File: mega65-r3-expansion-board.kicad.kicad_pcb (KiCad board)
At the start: 4 copper layers, 435 x 140.6 mm, 52 parts, among them J17 C64_Tape_Port, J18 BA60BC0WT, J19 C64_User_Port, J24 Component A/V, J32 Mini-DIN-8-With-Shield, J34 Conn_01x04, J35 Conn_01x04, U16 74LVC374, U17 74LVC374, U18 74LS374, U19 74LS374, U20 74LS125, U21 74LS125, U23 74LVC374, U24 74LS125, U25 74LS374, U26 74LS374

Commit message: begin placing and routing
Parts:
- removed J32: Mini-DIN-8-With-Shield, snapeda:mini-DIN-8
- removed R38: 510R, snapeda:Labeled Resistor
- removed R39: 1K0, snapeda:Labeled Resistor
- removed R40: 2K0, snapeda:Labeled Resistor
- removed R41: 4K0, snapeda:Labeled Resistor
- removed R42, R48, R54, R60: 8K0, snapeda:Labeled Resistor
- removed R43, R49, R55, R61: 16K, snapeda:Labeled Resistor
- removed U16, U17, U23: 74LVC374, snapeda:DIP-20_LVC_Family
- removed U18, U19, U25, U26: 74LS374, snapeda:DIP-20_LS_Family
- added J1: Mini-DIN-8-With-Shield, snapeda:mini-DIN-8, F.Cu at (168.2, 41.3)
- added J2: Conn_02x06_Odd_Even, Connector_PinHeader_2.54mm:PinHeader_2x06_P2.54mm_Vertical, F.Cu at (45.6, 123.1)
- added J3: Conn_02x06_Odd_Even, Connector_PinHeader_2.54mm:PinHeader_2x06_P2.54mm_Vertical, F.Cu at (68.5, 123.1)
- added J4: Conn_02x17_Odd_Even, Connector_PinHeader_2.54mm:PinHeader_2x17_P2.54mm_Vertical, F.Cu at (120.3, 132.7)
- added J5: Conn_02x17_Odd_Even, Connector_PinHeader_2.54mm:PinHeader_2x17_P2.54mm_Vertical, F.Cu at (129.0, 133.0)
- added R1: 3K3, snapeda:Labeled Resistor, F.Cu at (123.1, 74.5)
- added R2: 3K3, snapeda:Labeled Resistor, F.Cu at (29.1, 83.7)
- added R3: 3K3, snapeda:Labeled Resistor, F.Cu at (29.1, 93.7)
- added R4: 3K3, snapeda:Labeled Resistor, F.Cu at (29.1, 60.9)
- added R5: 3K3, snapeda:Labeled Resistor, F.Cu at (29.1, 70.8)
- added R6: 3K3, snapeda:Labeled Resistor, F.Cu at (123.1, 78.6)
- added U1: 74LS595, snapeda:DIP-16_LS_Family, F.Cu at (63.4, 87.5)
- added U2: 74LS165, snapeda:DIP-16_LVC_Family, F.Cu at (63.4, 71.5)
- added U4: 74LS595, snapeda:DIP-16_LS_Family, F.Cu at (88.8, 87.5)
- added U5: 74LS165, snapeda:DIP-16_LVC_Family, F.Cu at (35.5, 100.2)
- added U6: 74LS595, snapeda:DIP-16_LS_Family, F.Cu at (142.2, 54.5)
- added U7: 74LS165, snapeda:DIP-16_LVC_Family, F.Cu at (167.6, 54.5)
- added U8: 74LS595, snapeda:DIP-16_LS_Family, F.Cu at (35.5, 87.5)
- moved J34 252.7 mm to (44.4, 108.5)
- moved J35 248.1 mm to (62.2, 108.5)
- moved R50 222.1 mm to (113.7, 49.0)
- moved R51 222.1 mm to (113.7, 52.3)
- moved R52 222.1 mm to (113.7, 55.6)
- moved R53 222.1 mm to (113.7, 58.9)
- moved U24 222.1 mm to (41.0, 51.8)
- moved H10 222.1 mm to (34.9, 47.9)
- moved H11 222.1 mm to (94.9, 47.9)
- moved H12 222.1 mm to (112.9, 37.9)
- moved H13 222.1 mm to (142.9, 37.9)
- moved H14 222.1 mm to (153.9, 37.9)
- moved H15 222.1 mm to (182.9, 37.9)
- moved H16 222.1 mm to (34.9, 107.9)
- moved H17 222.1 mm to (94.9, 107.9)
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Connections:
- J24 pad 3: AUDIO_L -> AUDIO_R
- U20 pad 1: /User Port/EN_RESET_N -> /User Port/RESET_N_O
- U20 pad 11: unconnected-(U20-Pad11) -> 1565_SERIO
- U20 pad 12: unconnected-(U20-Pad12) -> 1565_SERIO_O
- U20 pad 13: GND -> EN_1565_SERIO
- U20 pad 2: /User Port/RESET_N_O -> GND
- U20 pad 4: GND -> /User Port/ATN_O
- U20 pad 5: unconnected-(U20-Pad5) -> GND
- U20 pad 6: unconnected-(U20-Pad6) -> IEC_ATN
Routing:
- net /User Port/6V_REG_CTL: track 283.1 -> 0.00 mm, vias 7 -> 0
- net /User Port/TAPE_WRITE: track 277.6 -> 12.3 mm, vias 8 -> 1
- net /User Port/TAPE_READ: track 206.6 -> 12.4 mm, vias 6 -> 1
- net +5V: track 545.0 -> 352.5 mm, vias 12 -> 5
- net /User Port/TAPE_SENSE: track 200.3 -> 12.4 mm, vias 6 -> 1
- net 1565_SERIO: track 176.3 -> 0.00 mm, vias 3 -> 0
- net AUDIO_L: track 159.6 -> 0.00 mm, vias 1 -> 0
- net /User Port/DATA_7: track 167.1 -> 14.4 mm, vias 6 -> 0
- net MUX_DO7: track 132.6 -> 0.00 mm
- net /User Port/DATA_6: track 160.4 -> 29.0 mm, vias 8 -> 4
- net /User Port/DATA_5: track 148.0 -> 18.4 mm, vias 8 -> 1
- net MUX_DO4: track 119.3 -> 0.00 mm, vias 2 -> 0
- net FL_WDATA: track 0.00 -> 117.1 mm
- net MUX_DO3: track 115.9 -> 0.00 mm, vias 4 -> 0
- net MUX_DO2: track 113.3 -> 0.00 mm, vias 2 -> 0
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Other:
- board size 435 x 140.6 mm -> 215 x 140.6 mm
- board text removed: "."
- board text removed: "0.47uF"
- board text removed: "1N5825"
- board text removed: "22uH"
- board text removed: "J4"
- board text removed: "X"

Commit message: route many signals
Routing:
- net +5V: track 352.5 -> 565.7 mm, vias 5 -> 23
- net /User Port/RESET_N: track 23.3 -> 197.7 mm, vias 3 -> 8
- net +3V3: track 0.00 -> 133.7 mm, vias 0 -> 3
- net /User Port/PC2: track 0.00 -> 124.3 mm, vias 0 -> 3
- net /User Port/CNT2: track 0.00 -> 109.5 mm, vias 0 -> 4
- net /User Port/FLAG2: track 0.00 -> 108.7 mm, vias 0 -> 1
- net /User Port/SP1: track 0.00 -> 107.4 mm, vias 0 -> 5
- net /User Port/SP2: track 0.00 -> 100.6 mm, vias 0 -> 4
- net /User Port/CNT1: track 0.00 -> 97.3 mm, vias 0 -> 2
- net IEC_ATN: track 0.00 -> 83.4 mm, vias 0 -> 2
- net /User Port/DATA_5_O: track 0.00 -> 78.8 mm, vias 0 -> 2
- net /User Port/DATA_7_O: track 0.00 -> 77.2 mm, vias 0 -> 2
- net /User Port/EN_DATA_5: track 0.00 -> 50.0 mm, vias 0 -> 1
- net /User Port/DATA_7: track 14.4 -> 62.9 mm, vias 0 -> 5
- net /User Port/DATA_5: track 18.4 -> 65.3 mm, vias 1 -> 2
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
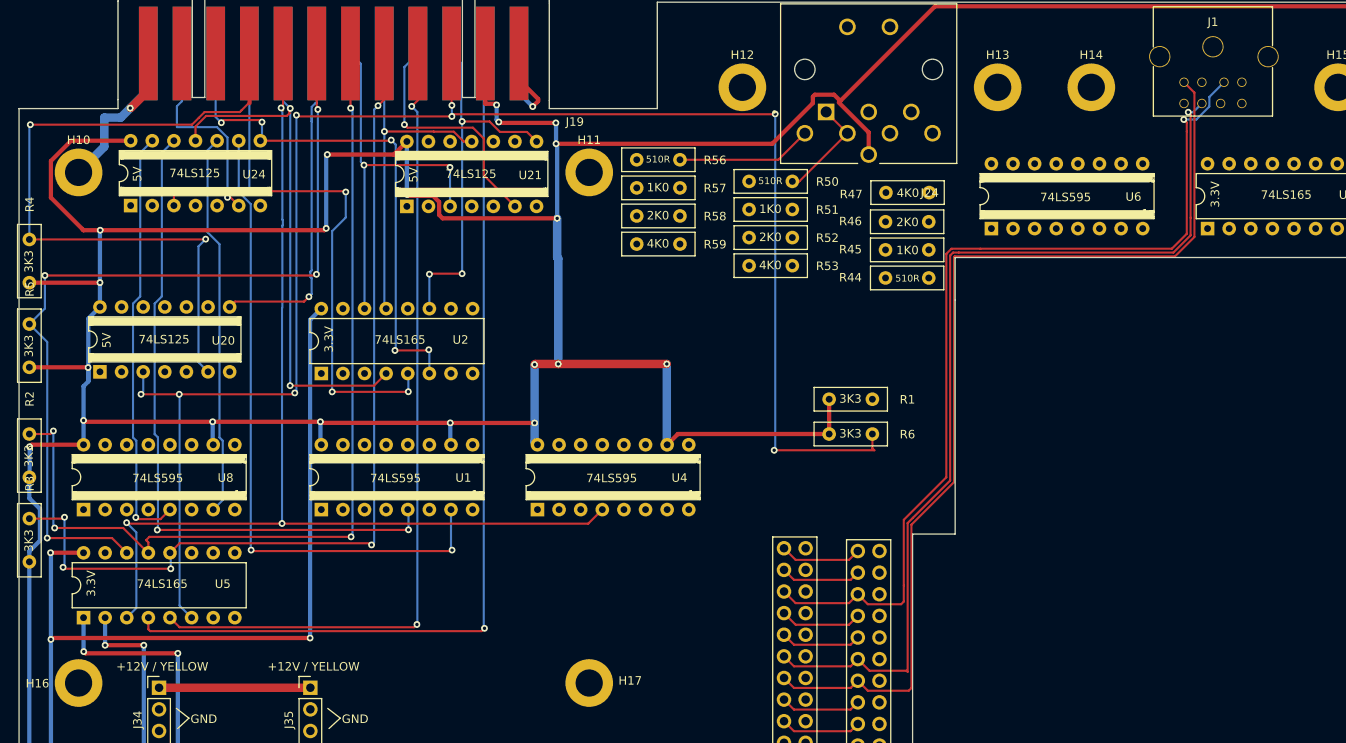
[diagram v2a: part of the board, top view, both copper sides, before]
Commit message: route many more signals
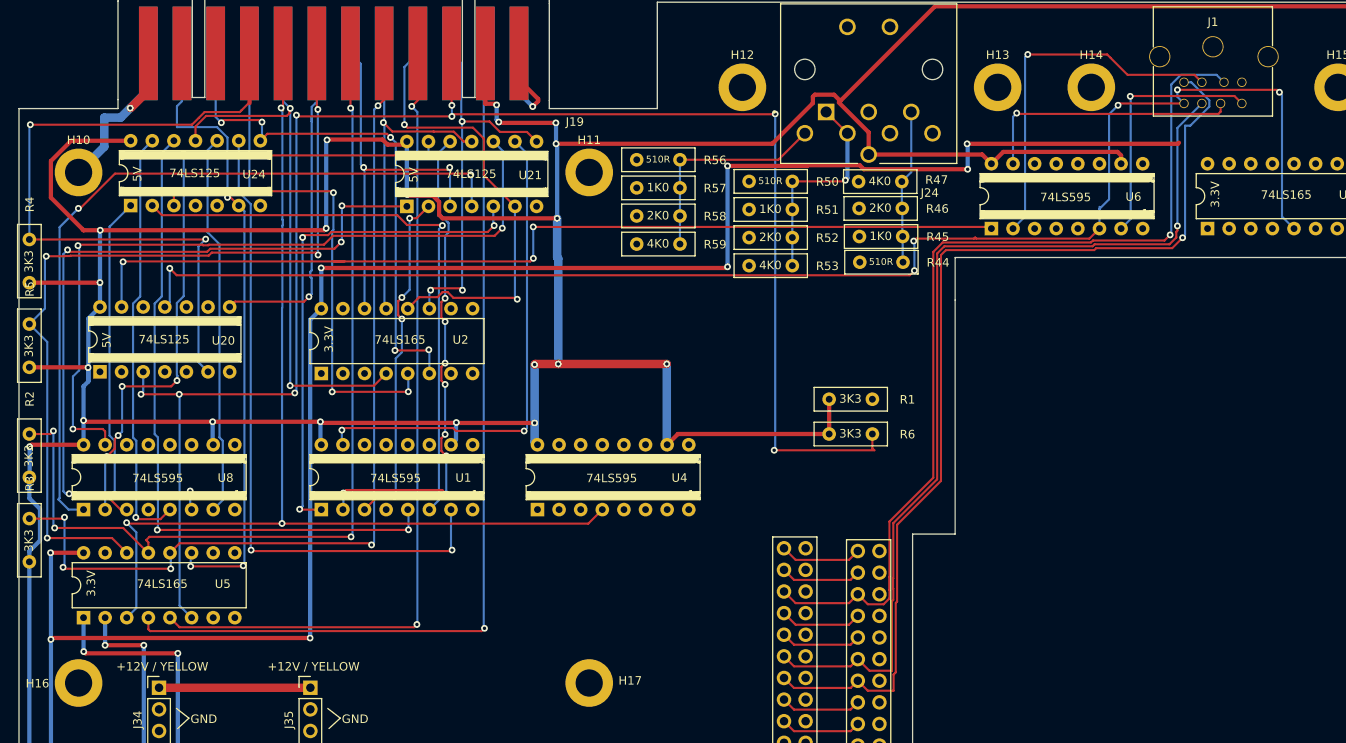
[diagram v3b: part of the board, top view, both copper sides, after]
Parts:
- moved R47 8.39 mm to (126.6, 49.0), turned to 0 degrees
- moved R46 8.34 mm to (126.6, 52.1), turned to 0 degrees
- moved R44 8.31 mm to (126.7, 58.4), turned to 0 degrees
- moved R45 8.29 mm to (126.7, 55.4), turned to 0 degrees
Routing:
- net 1565_SERIO: track 0.00 -> 173.1 mm, vias 0 -> 6
- net +3V3: track 133.7 -> 254.6 mm, vias 3 -> 8
- net EN_1565_SERIO: track 0.00 -> 112.8 mm, vias 0 -> 3
- net /User Port/EN_DATA_1: track 0.00 -> 90.4 mm, vias 0 -> 2
- net /User Port/EN_DATA_0: track 0.00 -> 88.8 mm, vias 0 -> 3
- net /User Port/EN_DATA_3: track 0.00 -> 81.6 mm, vias 0 -> 4
- net /User Port/EN_DATA_2: track 0.00 -> 79.5 mm, vias 0 -> 6
- net /User Port/DATA_6_O: track 0.00 -> 69.1 mm, vias 0 -> 1
- net /User Port/DATA_1_O: track 0.00 -> 60.0 mm, vias 0 -> 3
- net /User Port/DATA_2_O: track 0.00 -> 58.4 mm, vias 0 -> 8
- net /User Port/DATA_0_O: track 0.00 -> 58.2 mm, vias 0 -> 2
- net /User Port/PA2: track 24.1 -> 74.6 mm, vias 1 -> 3
- net /User Port/EN_DATA_6: track 0.00 -> 46.5 mm, vias 0 -> 2
- net 1565_RST: track 0.00 -> 43.0 mm, vias 0 -> 1
- net /User Port/DATA_3_O: track 0.00 -> 40.7 mm, vias 0 -> 4
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
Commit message: yet more routing
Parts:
- added U3: 74LS125, snapeda:DIP-14_74LS06, F.Cu at (88.7, 100.1)
- moved R3 2.61 mm to (29.7, 96.2)
- moved R4 2.31 mm to (29.9, 58.7)
- moved R5 1.17 mm to (30.0, 71.6)
- moved R2 0.77 mm to (29.9, 83.8)
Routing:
- net +12V_FUSED: track 17.3 -> 294.0 mm, vias 0 -> 6
- net EXP_RDATA: track 0.00 -> 274.1 mm, vias 0 -> 4
- net Net-(U5-Pad10): track 0.00 -> 217.0 mm, vias 0 -> 8
- net Net-(U6-Pad9): track 0.00 -> 158.4 mm, vias 0 -> 4
- net EXP_LATCH: track 34.2 -> 142.3 mm, vias 2 -> 10
- net EXP_CLOCK: track 27.6 -> 128.5 mm, vias 2 -> 9
- net /User Port/6V_REG_CTL: track 0.00 -> 98.4 mm, vias 0 -> 2
- net /User Port/RESET_N_O: track 0.00 -> 84.0 mm, vias 0 -> 2
- net /User Port/CNT1: track 97.3 -> 175.8 mm
- net /User Port/TAPE_WRITE: track 12.3 -> 88.8 mm, vias 1 -> 3
- net /User Port/SP2: track 100.9 -> 175.0 mm, vias 4 -> 7
- net /User Port/ATN_O: track 0.00 -> 70.9 mm, vias 0 -> 2
- net EXP_WDATA: track 0.00 -> 70.4 mm, vias 0 -> 3
- net /User Port/DATA_4_O: track 0.00 -> 59.6 mm, vias 0 -> 4
- net /User Port/TAPE_READ: track 12.4 -> 70.7 mm, vias 1 -> 3
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
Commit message: finish routing signals
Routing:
- net AUDIO_R2: track 0.00 -> 182.6 mm, vias 0 -> 2
- net AUDIO_R3: track 0.06 -> 179.9 mm, vias 0 -> 2
- net AUDIO_R4: track 0.00 -> 174.4 mm, vias 0 -> 2
- net AUDIO_R5: track 0.00 -> 168.6 mm, vias 0 -> 2
- net COMP_LUMA5: track 0.00 -> 139.1 mm, vias 0 -> 3
- net COMP_CHROMA3: track 0.00 -> 139.0 mm, vias 0 -> 4
- net COMP_CHROMA2: track 0.00 -> 138.9 mm, vias 0 -> 4
- net COMP_LUMA4: track 0.00 -> 135.3 mm, vias 0 -> 3
- net COMP_CHROMA4: track 0.00 -> 135.3 mm, vias 0 -> 4
- net COMP_LUMA3: track 0.00 -> 132.8 mm, vias 0 -> 3
- net COMP_CHROMA5: track 0.00 -> 131.0 mm, vias 0 -> 4
- net COMP_LUMA2: track 0.00 -> 127.1 mm, vias 0 -> 3
- net EXP_CLOCK: track 128.5 -> 214.4 mm, vias 9 -> 12
- net EXP_LATCH: track 142.3 -> 225.9 mm, vias 10 -> 14
- net /User Port/CNT1: track 175.8 -> 258.8 mm, vias 2 -> 6
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
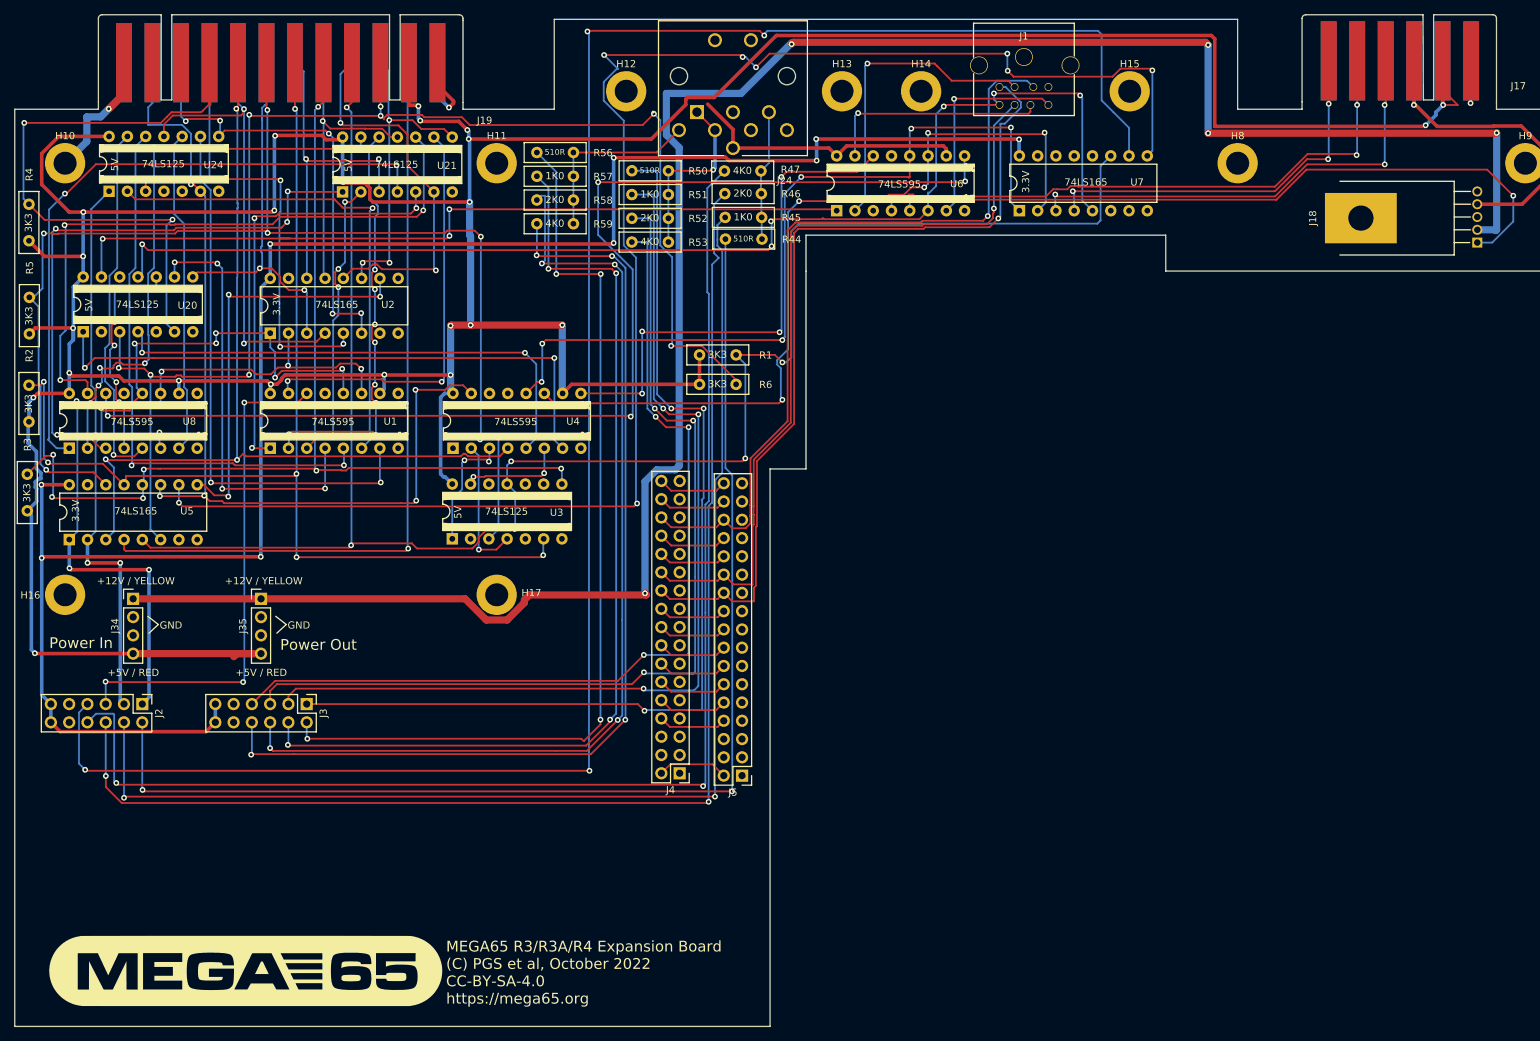
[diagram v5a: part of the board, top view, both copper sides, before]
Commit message: shrink board, resolve all DRC errors, add openhardware logo
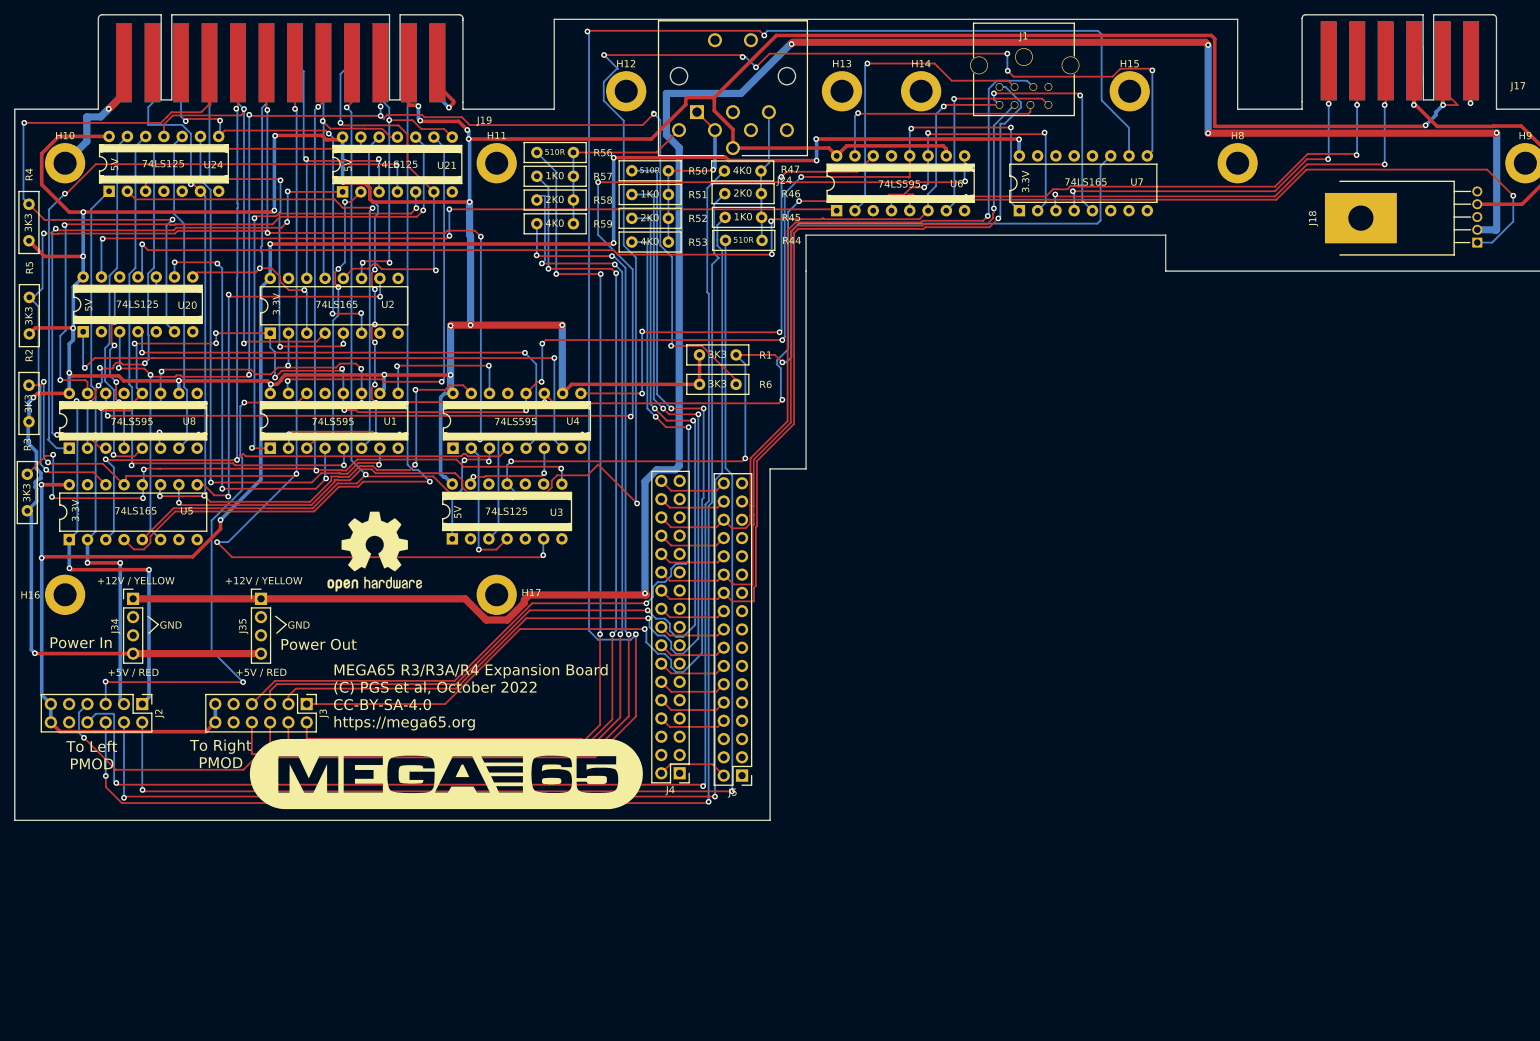
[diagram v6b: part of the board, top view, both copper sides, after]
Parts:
- added LOGO1: Logo_Open_Hardware_Large, Symbol:OSHW-Logo2_14.6x12mm_SilkScreen, F.Cu at (78.0, 101.9)
- moved G*** 39.1 mm to (87.9, 132.8)
- moved R44 0.18 mm to (126.7, 58.6)
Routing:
- net EXP_LATCH: track 225.9 -> 256.2 mm, vias 14 -> 16
- net EXP_CLOCK: track 214.4 -> 243.3 mm, vias 12 -> 14
- net Net-(U1-Pad9): track 0.00 -> 20.5 mm, vias 0 -> 2
- net /User Port/CNT2: track 156.3 -> 171.6 mm
- net /User Port/CNT1: track 258.8 -> 247.8 mm
- net Net-(U5-Pad10): track 225.7 -> 234.0 mm
- net EXP_RDATA: track 274.1 -> 281.0 mm
- net COMP_LUMA2: track 127.1 -> 120.9 mm
- net +3V3: track 260.2 -> 254.6 mm
- net EXP_WDATA: track 70.4 -> 74.3 mm
- net +5V: track 609.8 -> 606.0 mm
- net /User Port/PA2: track 128.6 -> 126.2 mm
- net COMP_LUMA4: track 135.3 -> 136.9 mm
- net /User Port/DATA_7_O: track 77.2 -> 75.7 mm
- net COMP_LUMA5: track 139.1 -> 140.6 mm
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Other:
- board size 215 x 140.6 mm -> 215 x 112 mm
- board text added: "To Left PMOD"
- board text added: "To Right PMOD"
